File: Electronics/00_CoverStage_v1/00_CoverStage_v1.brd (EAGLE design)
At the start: 100 x 80 mm, 0 parts

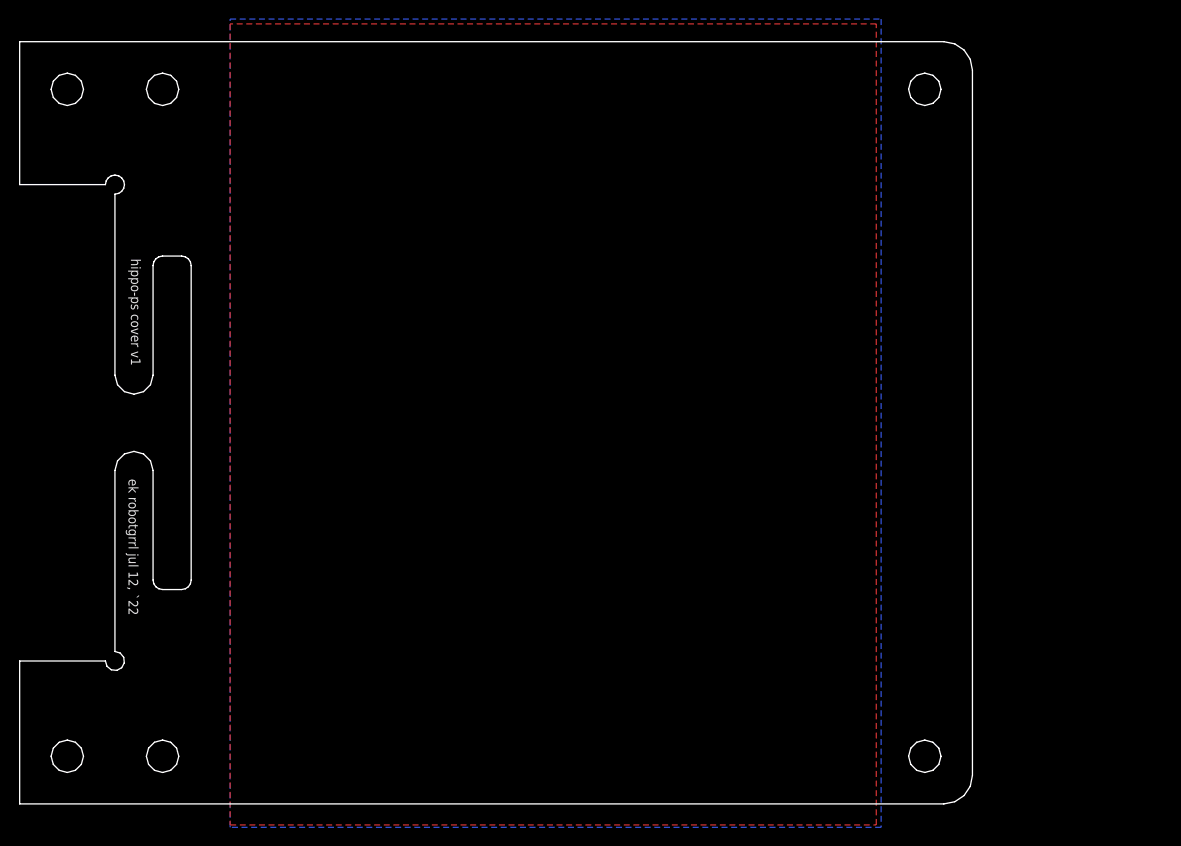
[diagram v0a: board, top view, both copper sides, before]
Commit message: Added handle to cover stage circuit board
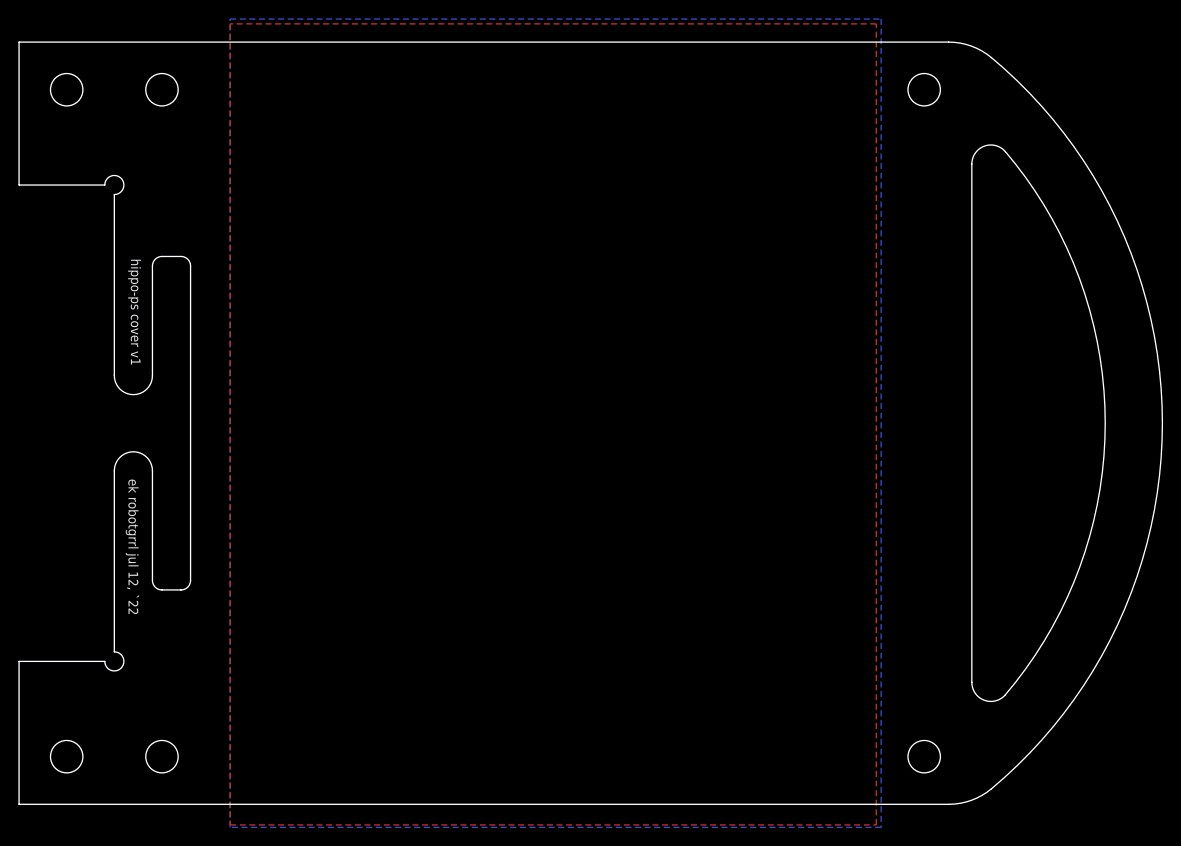
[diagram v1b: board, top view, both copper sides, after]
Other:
- board size 100 x 80 mm -> 120 x 80 mm

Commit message: Cover stage artwork naming update
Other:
- board text added: "hippo-pd cover v1"
- board text removed: "hippo-ps cover v1"
